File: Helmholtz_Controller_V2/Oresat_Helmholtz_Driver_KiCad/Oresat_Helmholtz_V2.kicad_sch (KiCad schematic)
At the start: 25 parts, among them U1 BDS63150AFM, U2 BDS63150AFM, U3 INA226, U4 INA226, U5 BDS63150AFM, U6 INA226, U7 RPi_Pico

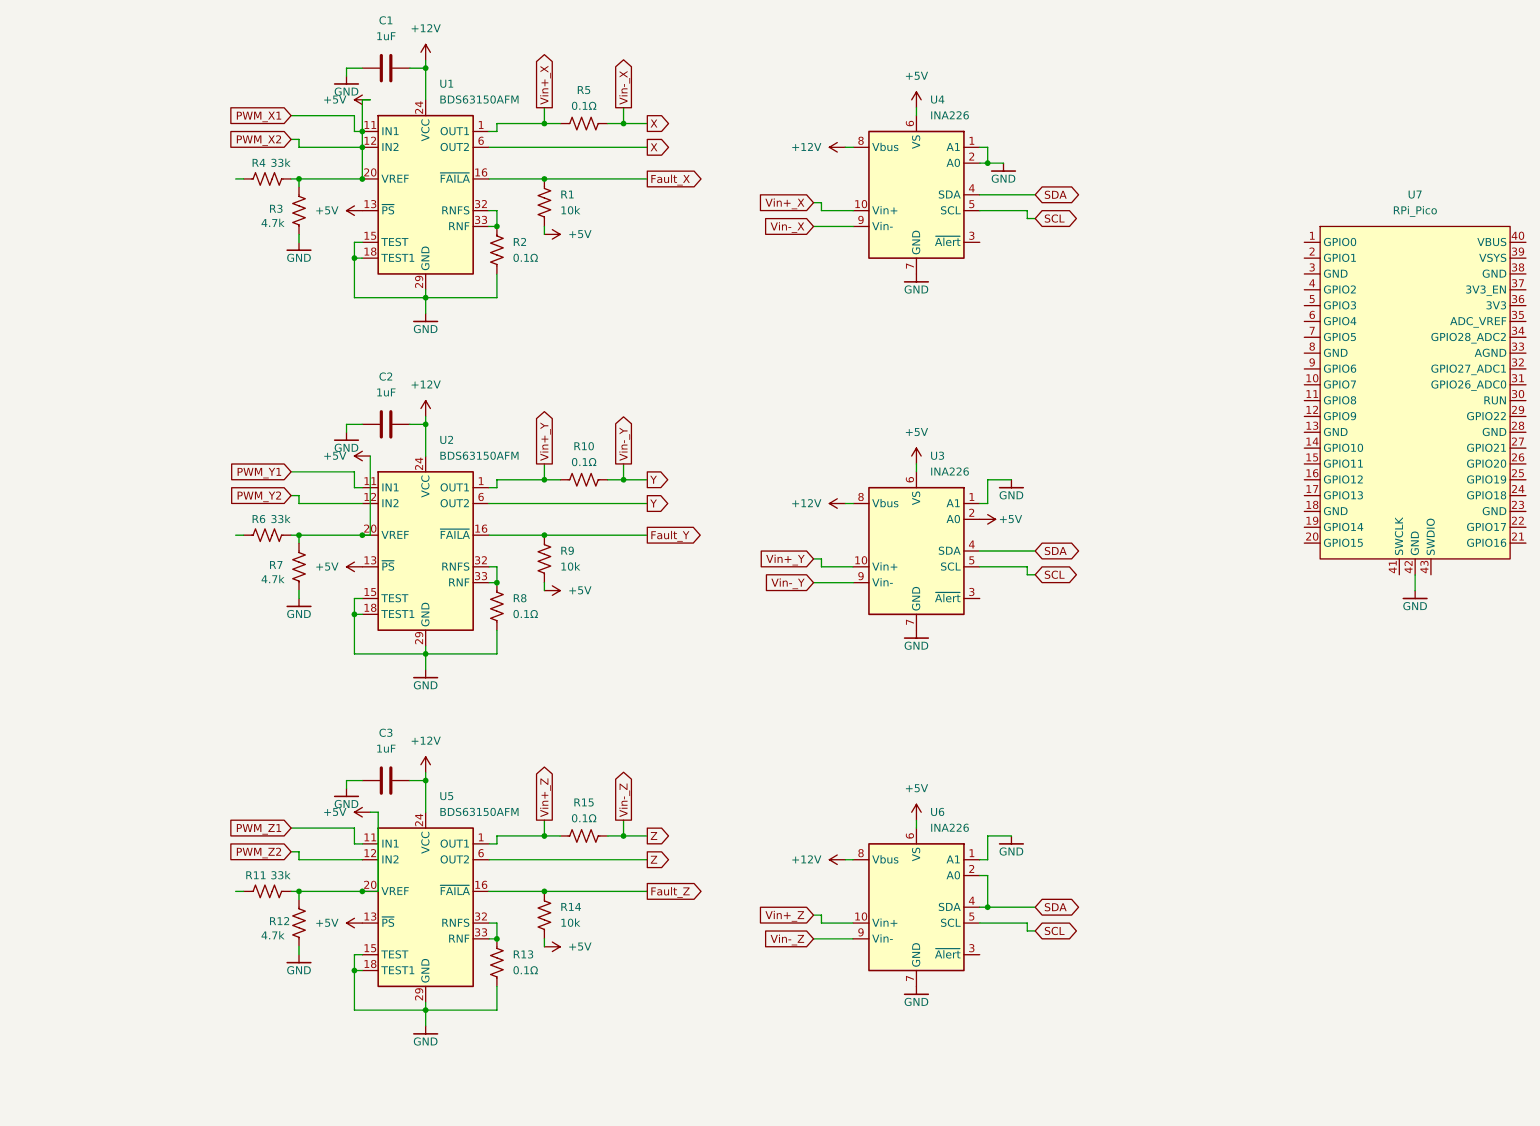
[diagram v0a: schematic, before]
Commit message: Added Helmholts Controller V2 with schematic
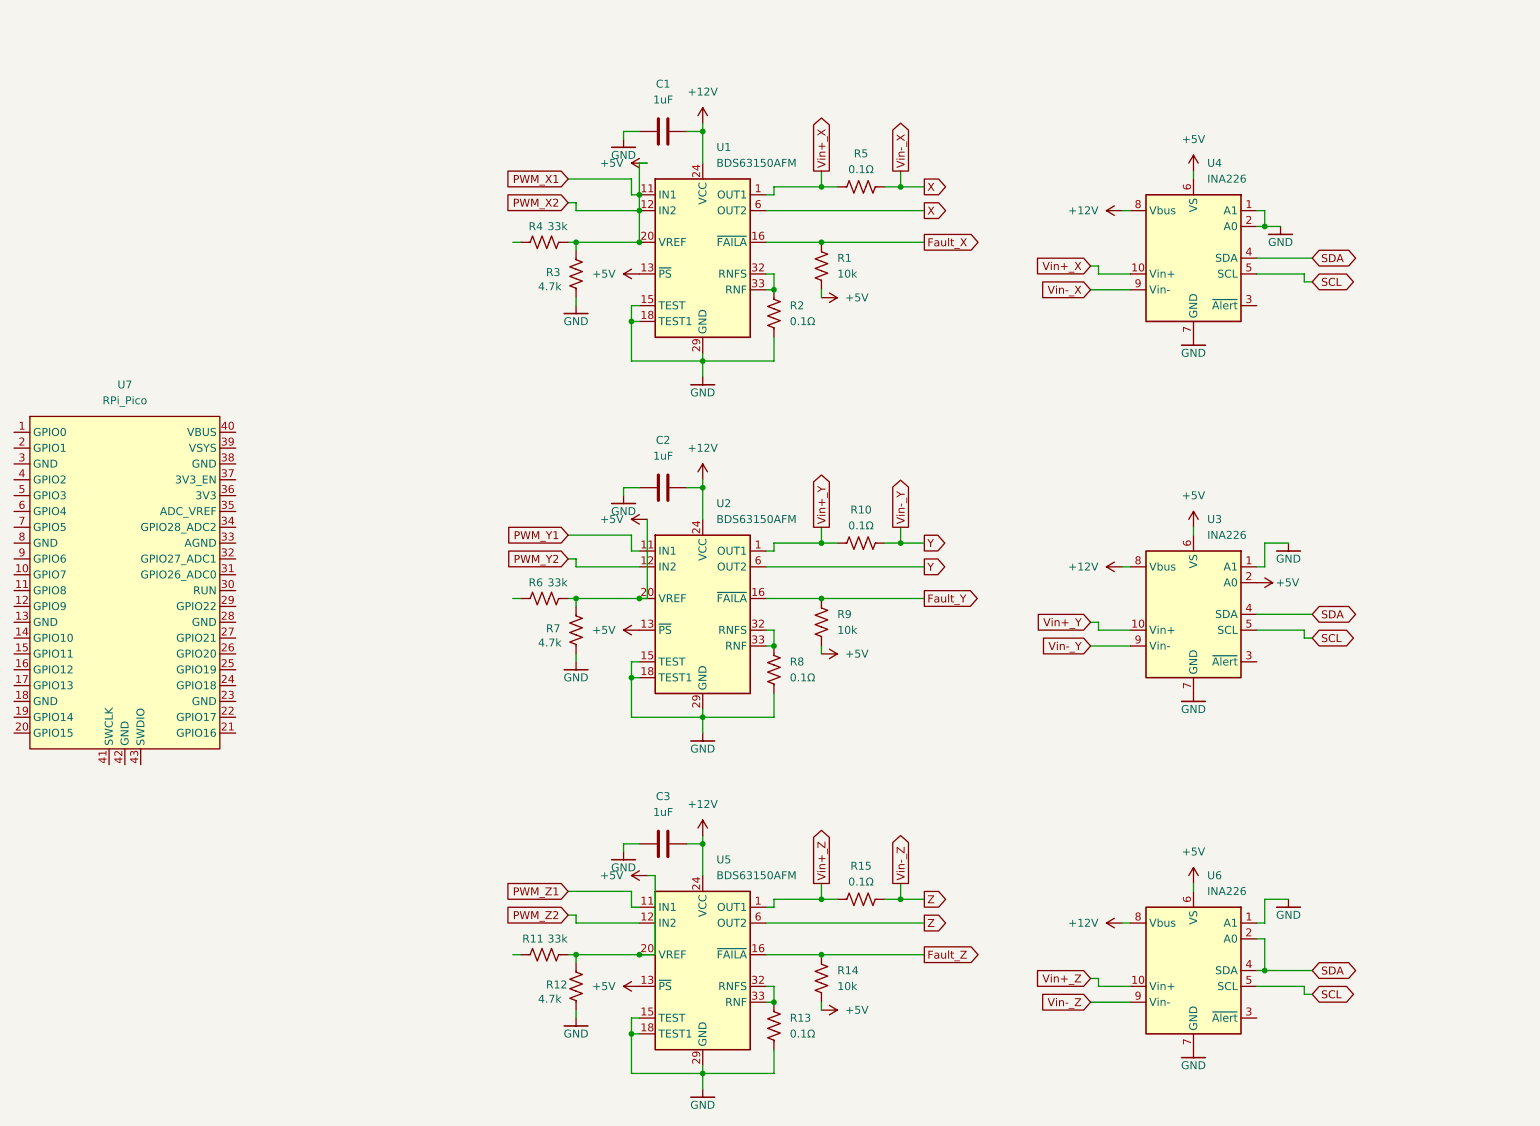
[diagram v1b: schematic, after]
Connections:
- net GND: no longer U7.42 (GND)
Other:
- moved on the sheet: C1, C2, C3, R1, R10, R11, R12, R13, R14, R15, R2, R3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
